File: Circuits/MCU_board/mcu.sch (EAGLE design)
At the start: 18 parts, among them U1 TCA9548APWR, U2 USBLC6-2P6, U3 LD39050PU33R, U5 STM32L452RECT6

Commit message: MCU changes
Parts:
- added C1, C2, C6: 0.1uF, SparkFun-Capacitors:0.1UF-0603-25V-(+80/-20%)
- added C7: 10nF, SparkFun-Capacitors:10NF-0603-50V-10%
- added C8: 10uF, SparkFun-Capacitors:10UF-0603-6.3V-20%
- added R1, R2, R3, R4: 10k, SparkFun-Resistors:10KOHM-0603-1/10W-1%
- added U$1, U$2, U$3, U$4, U$5: (no value), custom:MOLEX_522070633
- added U4: LSM9DS1, SparkFun-Sensors:LSM9DS1
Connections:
- new net C1: C1.1, U4.C1
- new net CAP: C7.1, U4.CAP
- new net CS_A/G: R2.1, U4.CS_A/G
- new net CS_M: R4.1, U4.CS_M
- new net SA0: R1.1, U4.SDO_A/G
- new net SA1: R3.1, U4.SDO_M
- new net SCL0: U$1.1, U1.SCL0
- new net SCL1: U$1.5, U$2.5, U1.SCL1
- new net SCL2: U$2.1, U1.SCL2
- new net SCL3: U$3.1, U1.SCL3
- new net SCL4: U$3.5, U$4.5, U1.SCL4
- new net SCL5: U$4.1, U1.SCL5
- new net SCL6: U$5.1, U1.SCL6
- new net SCL7: U$5.5, U1.SCL7, U4.SCL/SPC
- new net SDA0: U$1.2, U1.SDA0
- new net SDA1: U$1.6, U$2.6, U1.SDA1
- new net SDA2: U$2.2, U1.SDA2
- new net SDA3: U$3.2, U1.SDA3
- new net SDA4: U$3.6, U$4.6, U1.SDA4
- new net SDA5: U$4.2, U1.SDA5
- new net SDA6: U$5.2, U1.SDA6
- new net SDA7: U$5.6, U1.SDA7, U4.SDA/SDI/SDO
- net GND: now also C1.2, C2.2, C6.2, C7.2, C8.2, U$1.3, U$2.3, U$3.3, U$4.3, U$5.3, U4.GND, U4.RSVD
- net VCC: now also C2.1, C6.1, C8.1, R1.2, R2.2, R3.2, R4.2, U$1.4, U$2.4, U$3.4, U$4.4, U$5.4, U4.VDD, U4.VDDIO

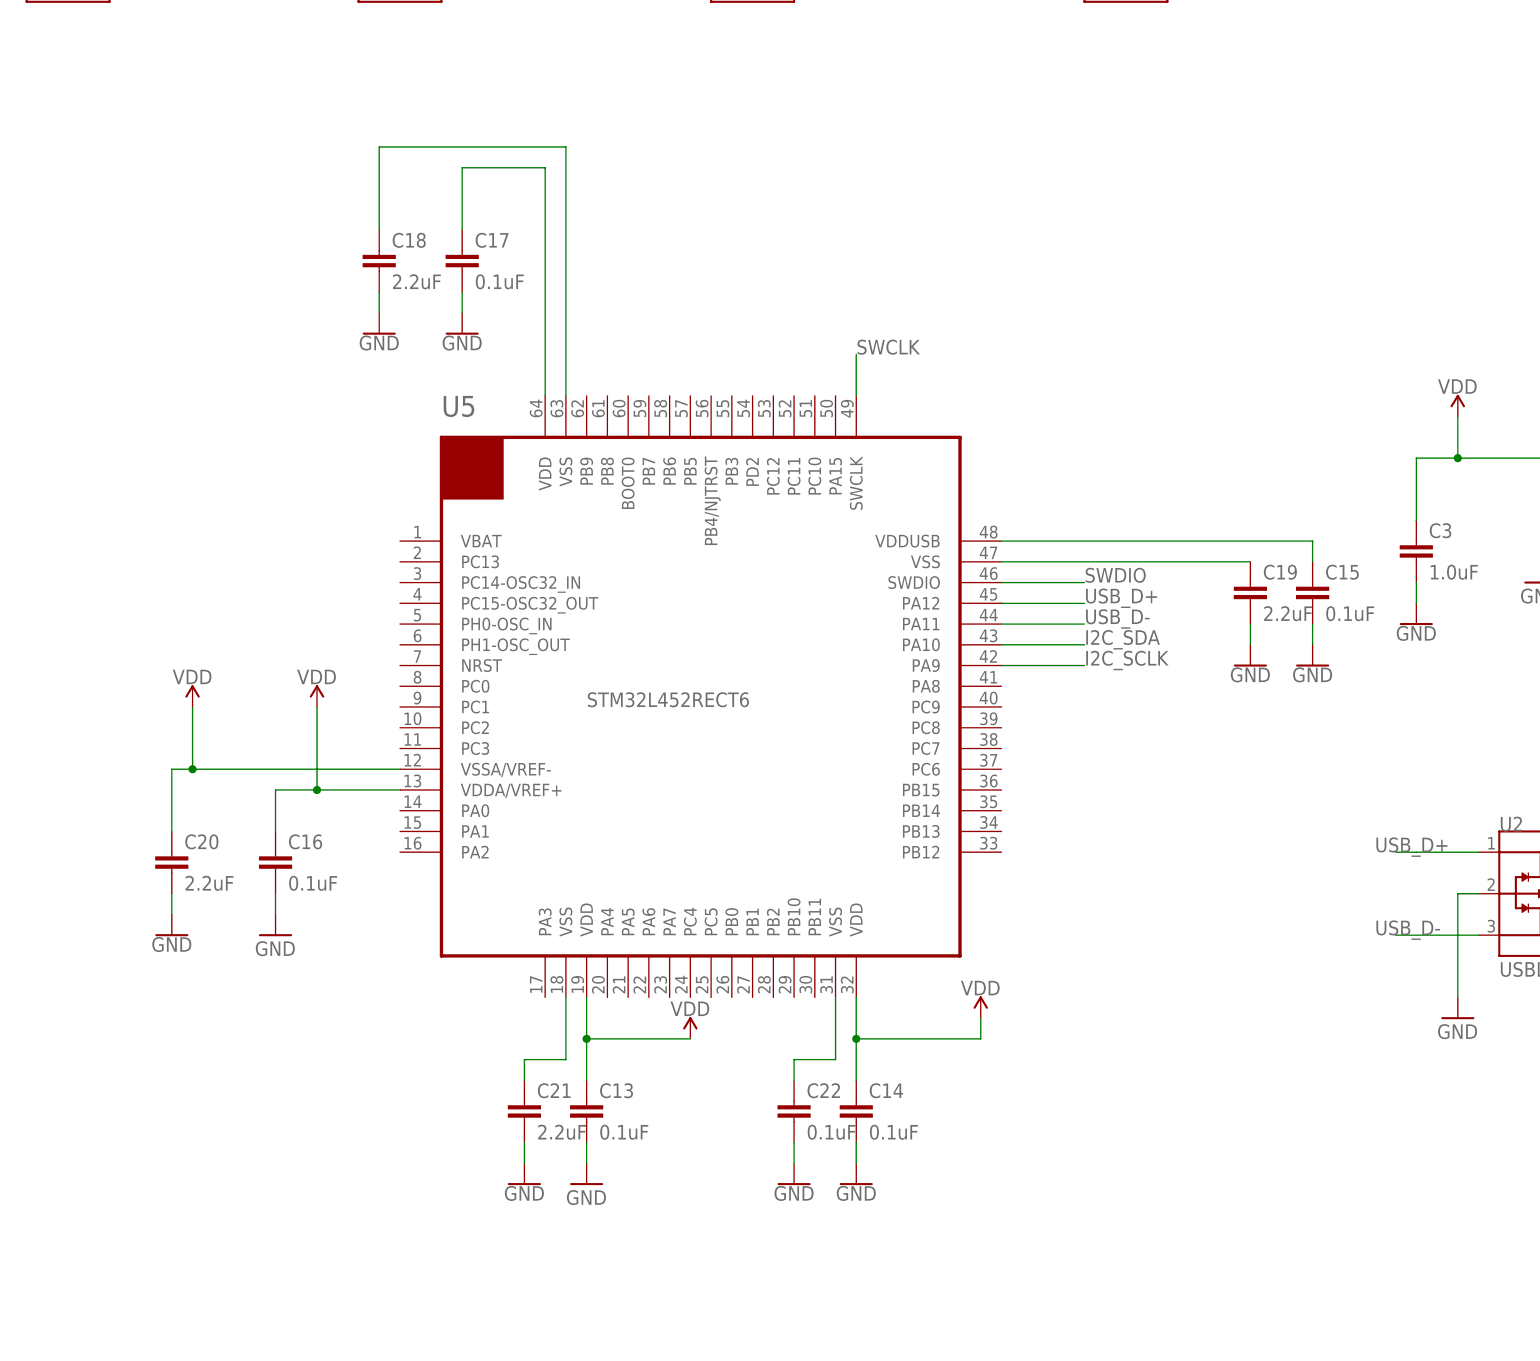
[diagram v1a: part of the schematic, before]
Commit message: Delete caps
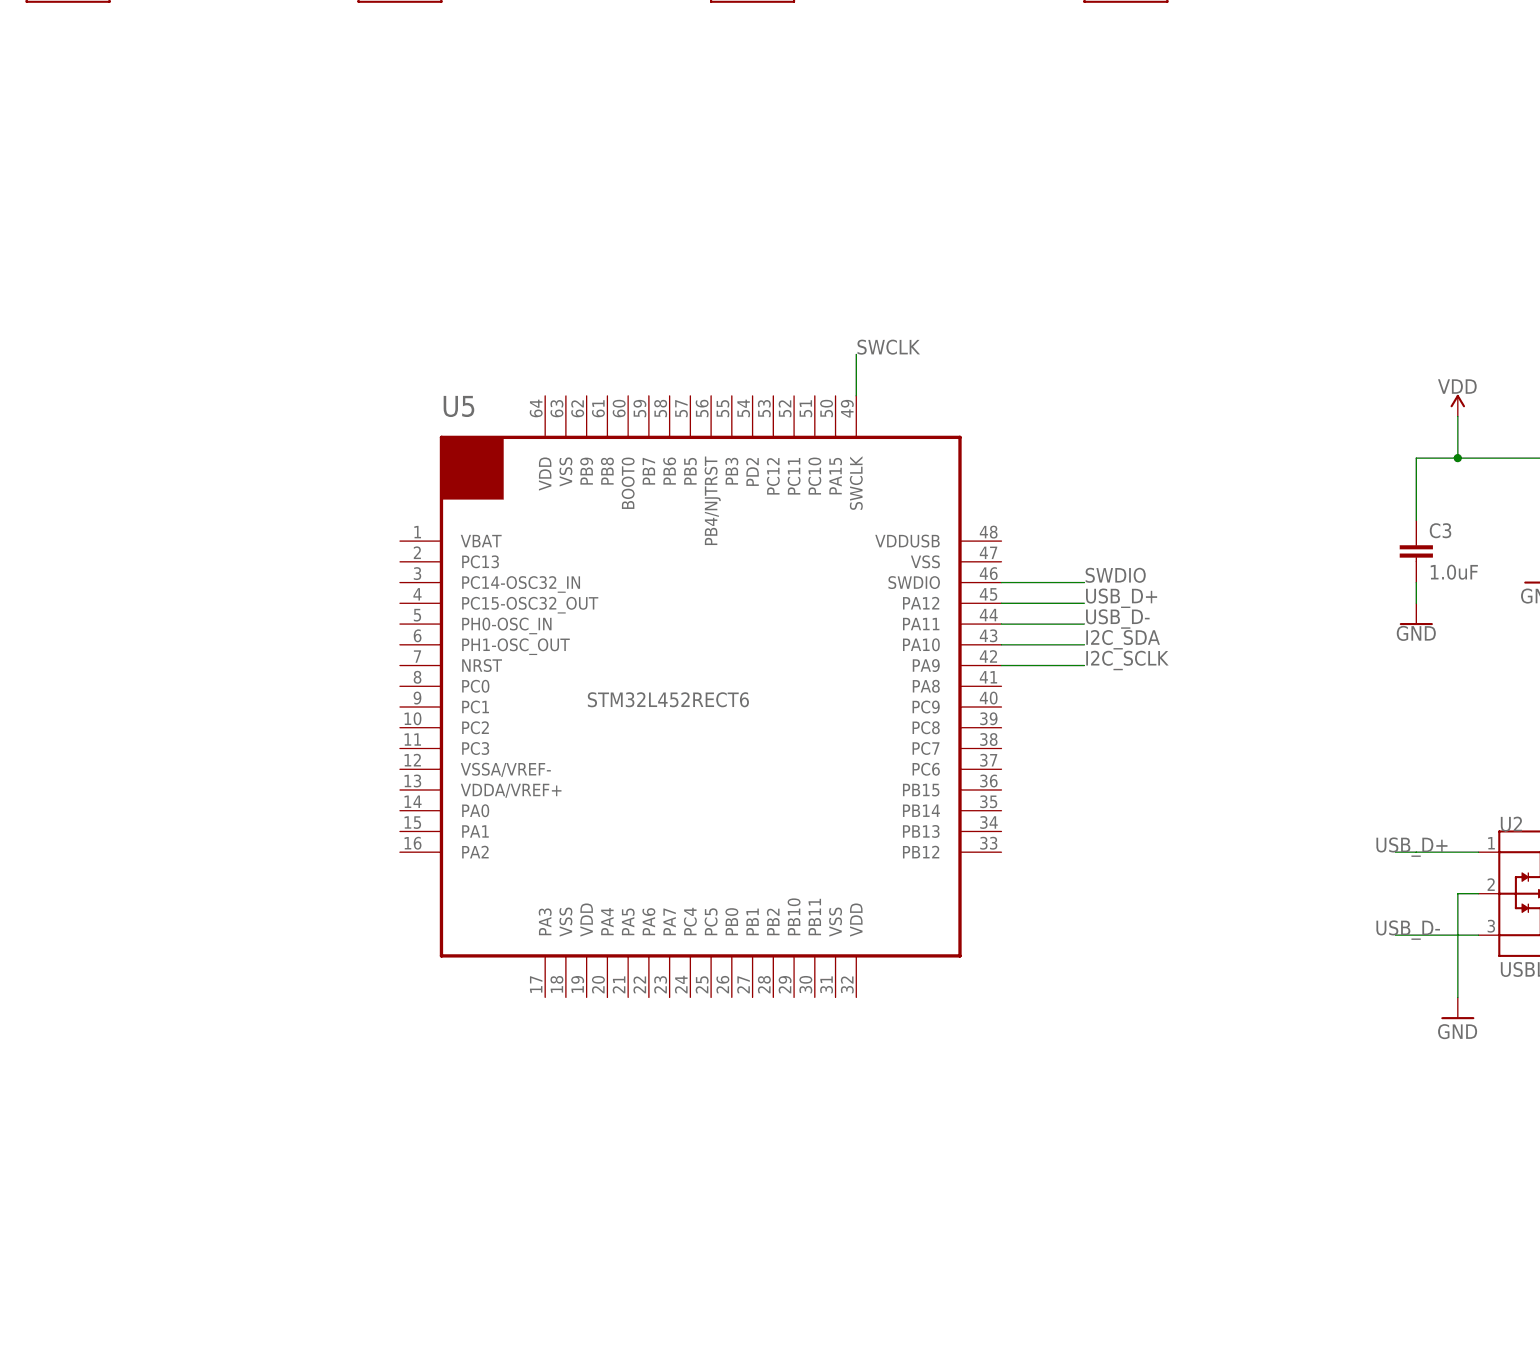
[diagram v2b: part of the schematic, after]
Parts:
- removed C13, C14, C15, C16, C17, C22: 0.1uF, SparkFun-Retired:.1UF-CER
- removed C18, C19, C20, C21: 2.2uF, SparkFun-Capacitors:2.2UF-0402_TIGHT-10V-10%-X5R
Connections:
- removed net N$21: C15.1, U5.VDDUSB
- removed net N$22: C19.1, U5.VSS@47
- removed net N$26: C21.1, U5.VSS@18
- removed net N$29: C17.1, U5.VDD@64
- removed net N$30: C18.1, U5.VSS@63
- removed net N$31: C22.1, U5.VSS@31
- net GND: no longer C13.2, C14.2, C15.2, C16.2, C17.2, C18.2, C19.2, C20.2, C21.2, C22.2
- net VDD: no longer C13.1, C14.1, C16.1, C20.1, U5.VDD@19, U5.VDD@32, U5.VDDA/VREF+, U5.VSSA/VREF-

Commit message: asdf
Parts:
- added C10, C12, C14, C16: 4.7uF, SparkFun-Capacitors:0.18UF-0603-10V-10%
- added C11, C13, C15, C9: 100nF, SparkFun-Capacitors:0.18UF-0603-10V-10%
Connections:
- net GND: now also C10.2, C11.2, C12.2, C13.2, C14.2, C15.2, C16.2, C9.2, U5.VSS@18, U5.VSS@31, U5.VSS@47, U5.VSS@63
- net VDD: now also C10.1, C11.1, C12.1, C13.1, C14.1, C15.1, C16.1, C9.1, U5.VDD@19, U5.VDD@32, U5.VDD@64, U5.VDDUSB
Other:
- moved on the sheet: U$1, U$2, U$3, U$4, U$5

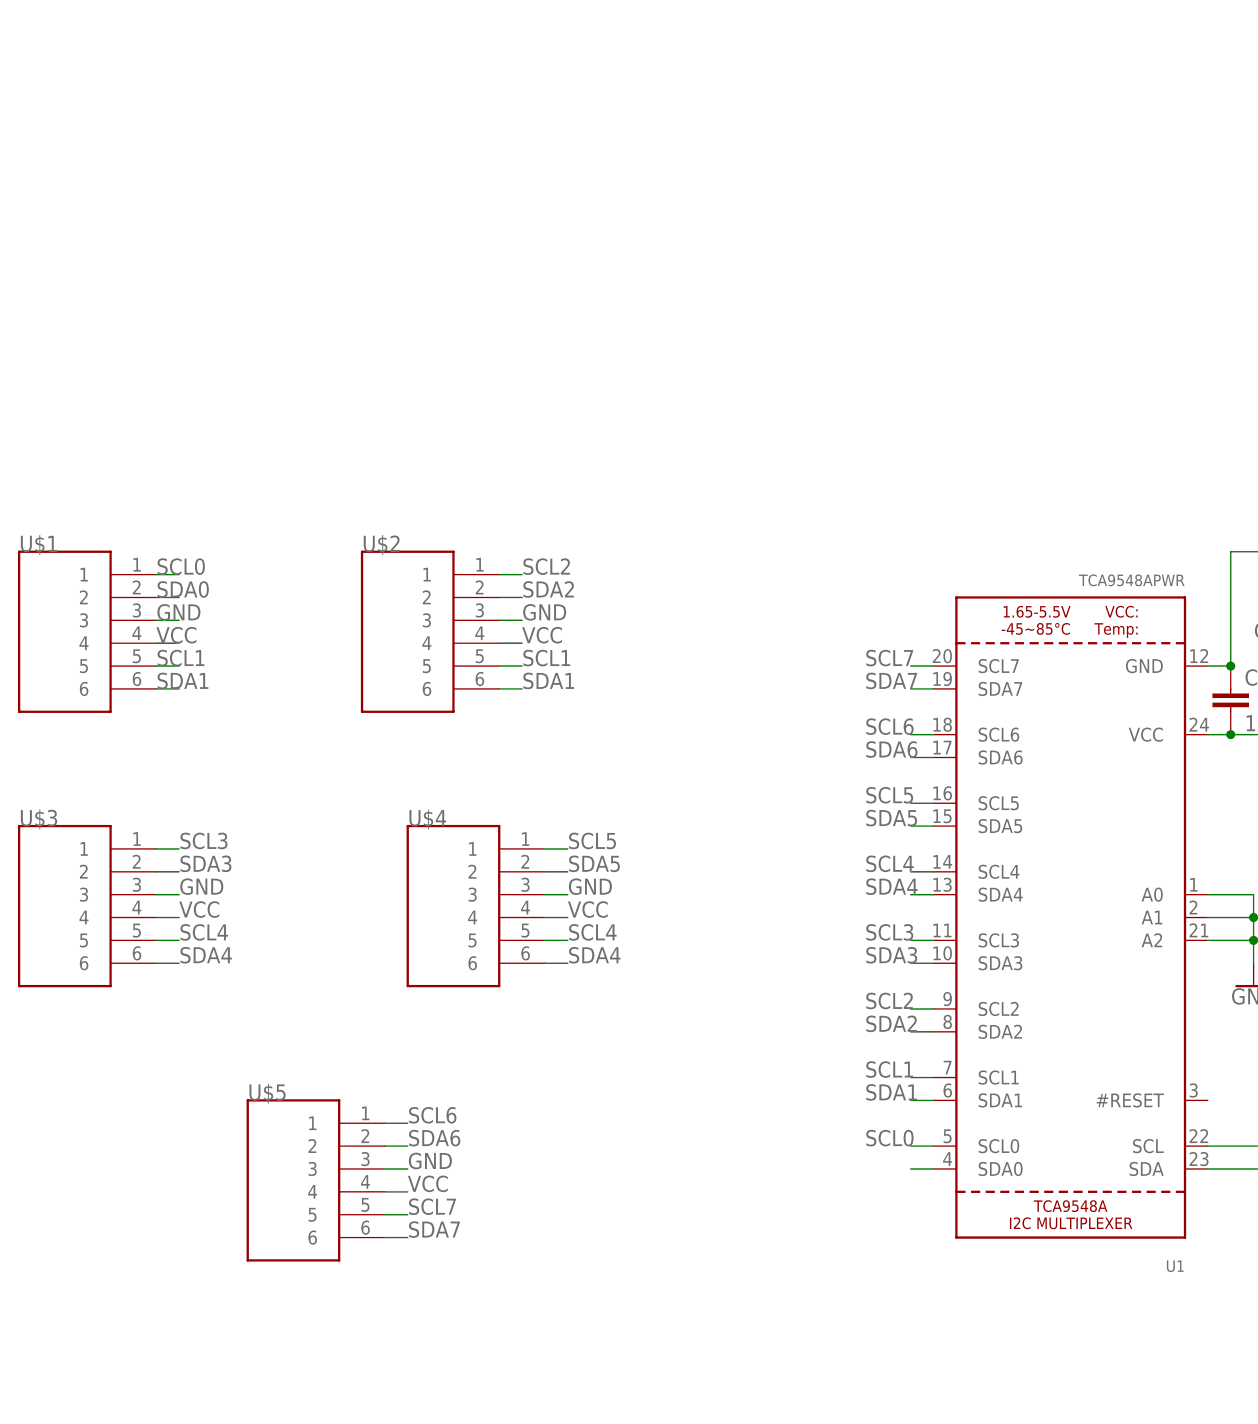
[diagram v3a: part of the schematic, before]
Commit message: Add connectors on mcu board
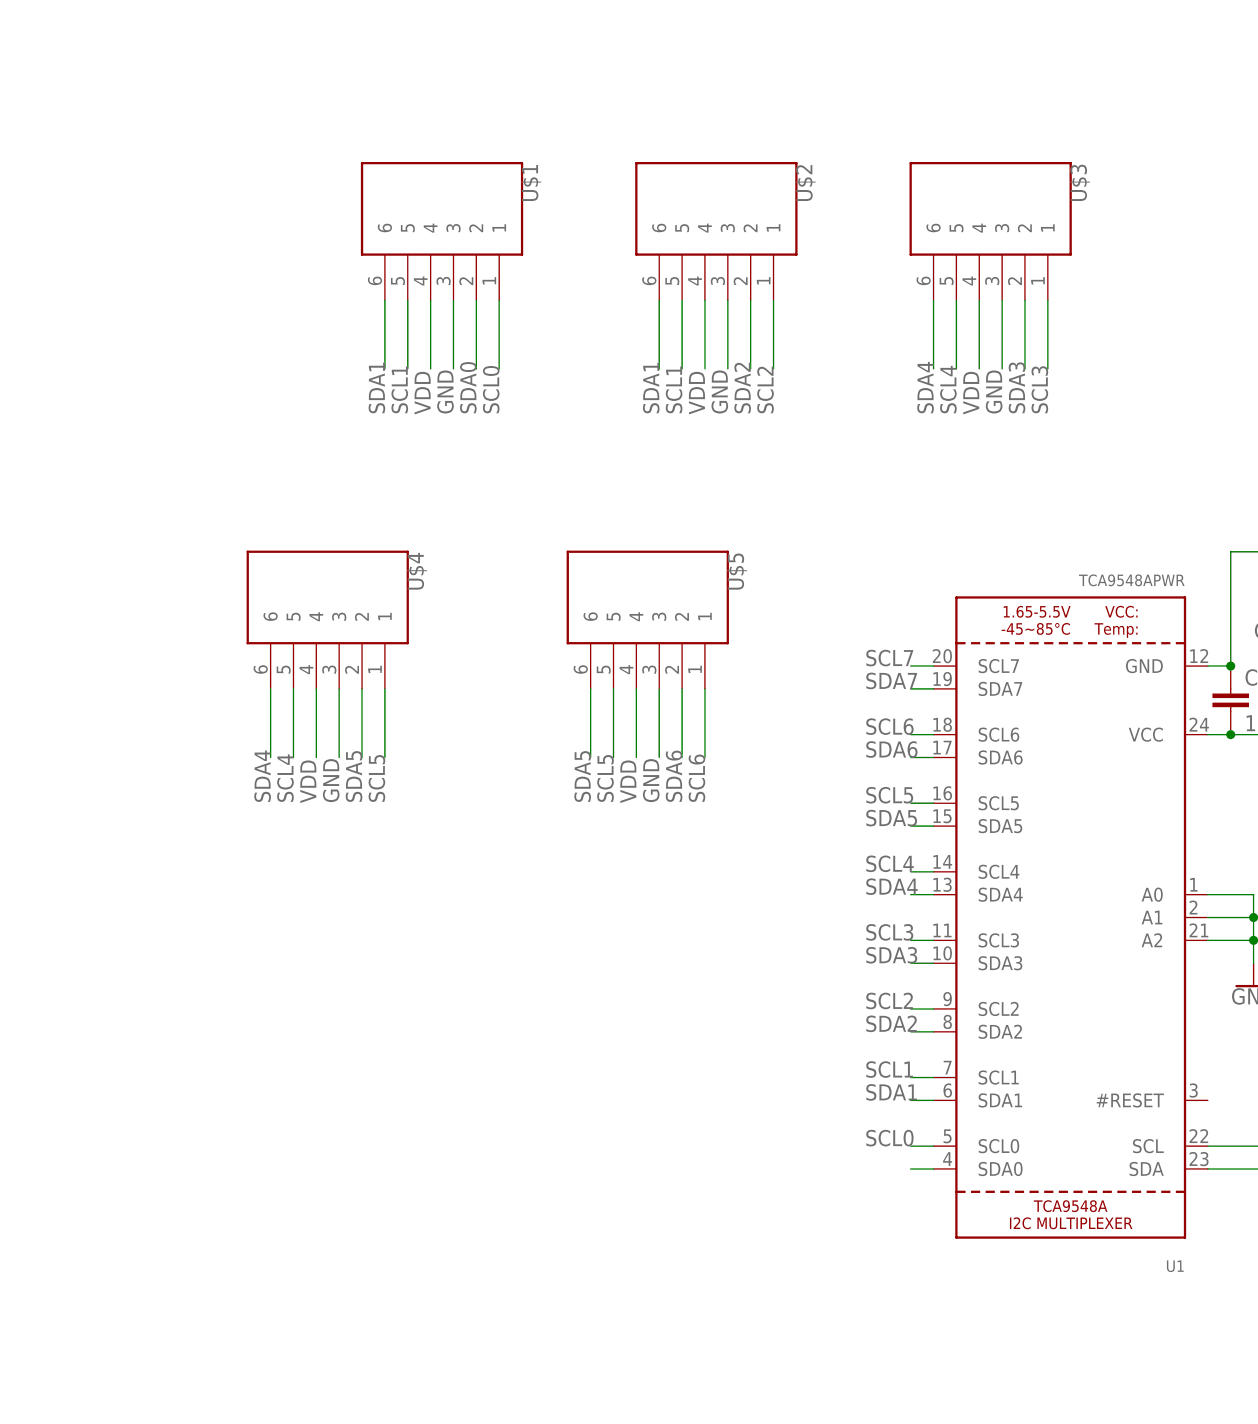
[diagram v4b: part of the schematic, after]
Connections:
- net SCL5: now also U$5.5
- net SCL7: no longer U$5.5
- net SDA5: now also U$5.6
- net SDA7: no longer U$5.6
- net VCC: no longer U$1.4, U$2.4, U$3.4, U$4.4, U$5.4
- net VDD: now also U$1.4, U$2.4, U$3.4, U$4.4, U$5.4
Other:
- moved on the sheet: U$1, U$2, U$3, U$4, U$5
